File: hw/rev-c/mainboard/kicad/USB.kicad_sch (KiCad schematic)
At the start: 6 parts, among them J24 USB1.1_HOST_TYPE_C

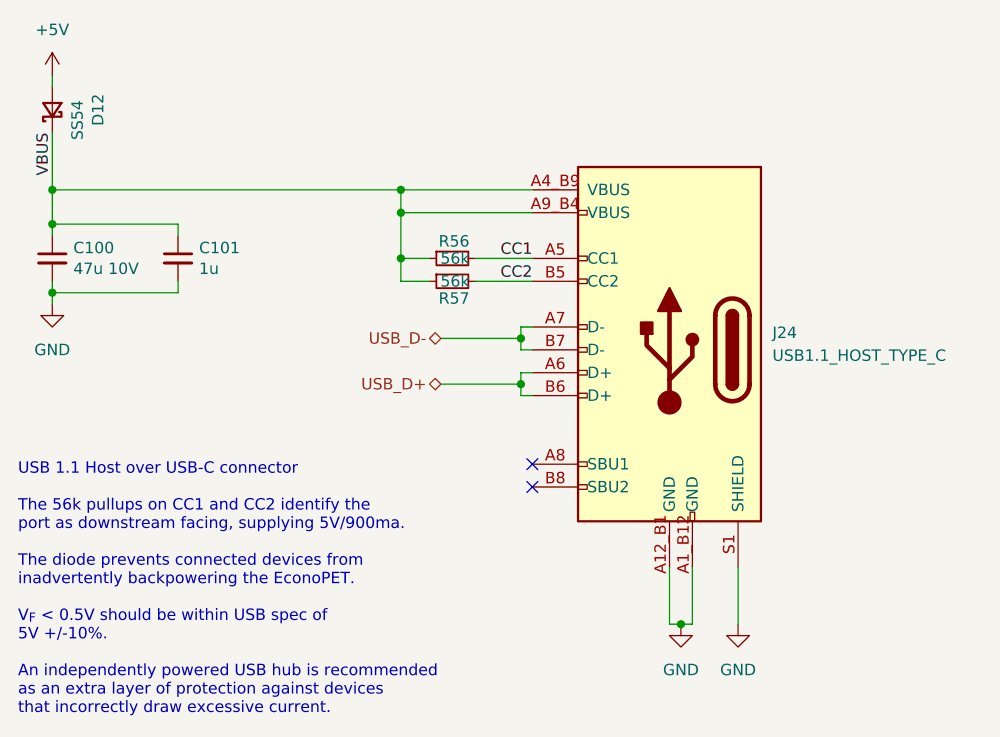
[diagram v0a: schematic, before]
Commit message: hw: fix wire/grid violations in schematic
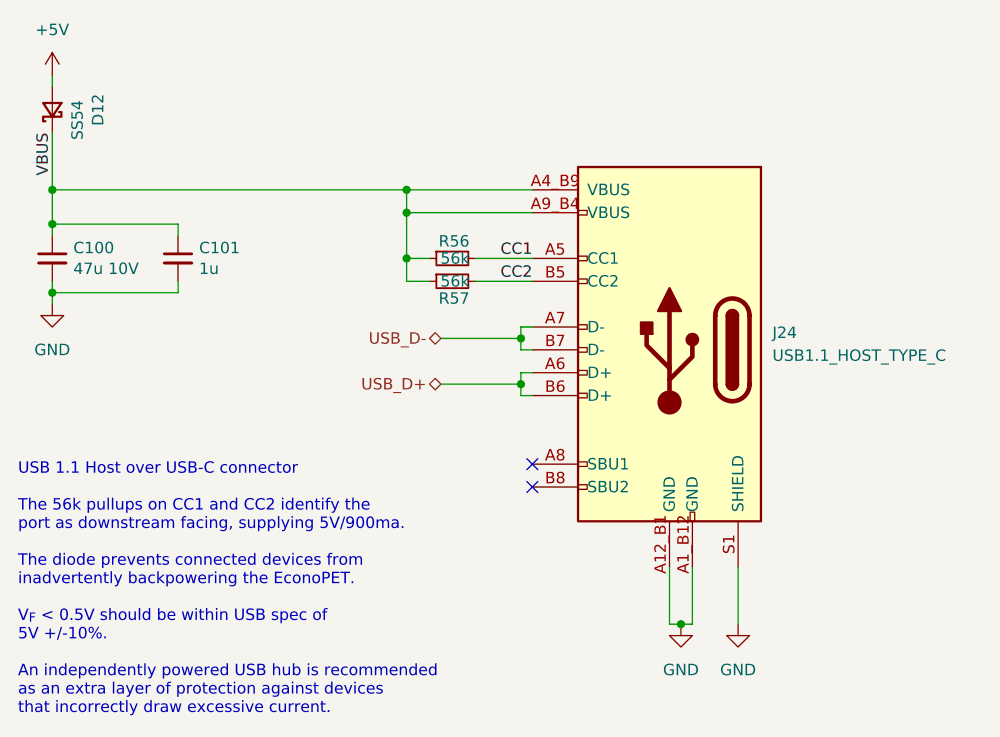
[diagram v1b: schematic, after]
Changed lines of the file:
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@@
+	)
+	(junction
+		(at 123.19 82.55)
+		(diameter 0)
+		(color 0 0 0 0)
 	)
 	(junction
@@
 	)
 	(junction
-		(at 122.555 77.47)
+		(at 123.19 77.47)
 		(diameter 0)
 		(color 0 0 0 0)
@@
 	)
 	(junction
-		(at 122.555 82.55)
-		(diameter 0)
-		(color 0 0 0 0)
-	)
-	(junction
-		(at 122.555 74.93)
+		(at 123.19 74.93)
 		(diameter 0)
 		(color 0 0 0 0)
@@
 	(wire
 		(pts
+			(xy 123.19 74.93) (xy 137.16 74.93)
+		)
+		(stroke
+			(width 0)
+			(type default)
+		)
+	)
+	(wire
+		(pts
 			(xy 137.16 95.25) (xy 135.89 95.25)
 		)
@@
 	(wire
 		(pts
-			(xy 122.555 77.47) (xy 137.16 77.47)
+			(xy 123.19 82.55) (xy 125.73 82.55)
 		)
 		(stroke
@@
 	(wire
 		(pts
-			(xy 122.555 82.55) (xy 122.555 77.47)
+			(xy 123.19 82.55) (xy 123.19 77.47)
 		)
 		(stroke
@@
 	(wire
 		(pts
-			(xy 83.82 74.93) (xy 122.555 74.93)
+			(xy 83.82 74.93) (xy 123.19 74.93)
 		)
 		(stroke
@@
 	(wire
 		(pts
-			(xy 122.555 85.09) (xy 122.555 82.55)
-		)
-		(stroke
-			(width 0)
-			(type default)
-		)
-	)
-	(wire
-		(pts
-			(xy 122.555 82.55) (xy 125.73 82.55)
+			(xy 123.19 85.09) (xy 123.19 82.55)
+		)
+		(stroke
+			(width 0)
+			(type default)
+		)
+	)
+	(wire
+		(pts
+			(xy 123.19 77.47) (xy 137.16 77.47)
 		)
 		(stroke
@@
 	(wire
 		(pts
-			(xy 122.555 77.47) (xy 122.555 74.93)
+			(xy 123.19 77.47) (xy 123.19 74.93)
 		)
 		(stroke
@@
 	(wire
 		(pts
-			(xy 122.555 74.93) (xy 137.16 74.93)
-		)
-		(stroke
-			(width 0)
-			(type default)
-		)
-	)
-	(wire
-		(pts
 			(xy 153.67 123.19) (xy 154.94 123.19)
 		)
@@
 	(wire
 		(pts
-			(xy 125.73 85.09) (xy 122.555 85.09)
-		)
-		(stroke
+			(xy 125.73 85.09) (xy 123.19 85.09)
+		)
+		(stroke

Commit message: hw: update usb-c receptical symbol
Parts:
- J24: symbol JLCPCB:USB_C_Receptacle_USB2.0 -> EconoPET:USB_C_Receptacle_USB2.0
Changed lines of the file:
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@@
 	)
 	(symbol
-		(lib_id "JLCPCB:USB_C_Receptacle_USB2.0")
+		(lib_id "EconoPET:USB_C_Receptacle_USB2.0")
 		(at 152.4 92.71 0)
 		(mirror y)

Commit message: hw: renumber reference designators
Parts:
- renumbered C100 to C101, C101 to C102, J24 to J25, R56 to R61, R57 to R62
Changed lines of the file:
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@@
 		(on_board yes)
 		(dnp no)
-		(property "Reference" "C101"
+		(property "Reference" "C102"
 			(at 100.1268 81.3816 0)
 			(effects
@@
 			(project ""
 				(path "/2eea20e6-112c-411a-b615-885ae773135a/00000000-0000-0000-0000-0000617d6918/b70241ab-8a5c-42d5-a1ab-8f4bc50a1197/6521fafb-cb3f-4004-93ad-439f568f7908"
-					(reference "C101")
+					(reference "C102")
 					(unit 1)
 				)
@@
 		(dnp no)
 		(fields_autoplaced yes)
-		(property "Reference" "#PWR0171"
+		(property "Reference" "#PWR0172"
 			(at 83.82 93.98 0)
 			(effects
@@
 			(project ""
 				(path "/2eea20e6-112c-411a-b615-885ae773135a/00000000-0000-0000-0000-0000617d6918/b70241ab-8a5c-42d5-a1ab-8f4bc50a1197/6521fafb-cb3f-4004-93ad-439f568f7908"
-					(reference "#PWR0171")
+					(reference "#PWR0172")
 					(unit 1)
 				)
@@
 		(dnp no)
 		(fields_autoplaced yes)
-		(property "Reference" "J24"
+		(property "Reference" "J25"
 			(at 163.83 90.8049 0)
 			(effects
@@
 			(project ""
 				(path "/2eea20e6-112c-411a-b615-885ae773135a/00000000-0000-0000-0000-0000617d6918/b70241ab-8a5c-42d5-a1ab-8f4bc50a1197/6521fafb-cb3f-4004-93ad-439f568f7908"
-					(reference "J24")
+					(reference "J25")
 					(unit 1)
 				)
@@
 		(on_board yes)
 		(dnp no)
-		(property "Reference" "R57"
+		(property "Reference" "R62"
 			(at 130.175 86.995 90)
 			(effects
@@
 			(project ""
 				(path "/2eea20e6-112c-411a-b615-885ae773135a/00000000-0000-0000-0000-0000617d6918/b70241ab-8a5c-42d5-a1ab-8f4bc50a1197/6521fafb-cb3f-4004-93ad-439f568f7908"
-					(reference "R57")
+					(reference "R62")
 					(unit 1)
 				)
@@
 		(on_board yes)
 		(dnp no)
-		(property "Reference" "C100"
+		(property "Reference" "C101"
 			(at 86.1568 81.3816 0)
 			(effects
@@
 			(project ""
 				(path "/2eea20e6-112c-411a-b615-885ae773135a/00000000-0000-0000-0000-0000617d6918/b70241ab-8a5c-42d5-a1ab-8f4bc50a1197/6521fafb-cb3f-4004-93ad-439f568f7908"
-					(reference "C100")
+					(reference "C101")
 					(unit 1)
 				)
@@
 		(dnp no)
 		(fields_autoplaced yes)
-		(property "Reference" "#PWR0170"
+		(property "Reference" "#PWR0171"
 			(at 83.82 66.04 0)
 			(effects
@@
 			(project ""
 				(path "/2eea20e6-112c-411a-b615-885ae773135a/00000000-0000-0000-0000-0000617d6918/b70241ab-8a5c-42d5-a1ab-8f4bc50a1197/6521fafb-cb3f-4004-93ad-439f568f7908"
-					(reference "#PWR0170")
+					(reference "#PWR0171")
 					(unit 1)
 				)
@@
 		(on_board yes)
 		(dnp no)
-		(property "Reference" "R56"
+		(property "Reference" "R61"
 			(at 130.175 80.645 90)
 			(effects
@@
 			(project ""
 				(path "/2eea20e6-112c-411a-b615-885ae773135a/00000000-0000-0000-0000-0000617d6918/b70241ab-8a5c-42d5-a1ab-8f4bc50a1197/6521fafb-cb3f-4004-93ad-439f568f7908"
-					(reference "R56")
+					(reference "R61")
 					(unit 1)
 				)
@@
 		(dnp no)
 		(fields_autoplaced yes)
-		(property "Reference" "#PWR0172"
+		(property "Reference" "#PWR0173"
 			(at 153.67 129.54 0)
 			(effects
@@
 			(project ""
 				(path "/2eea20e6-112c-411a-b615-885ae773135a/00000000-0000-0000-0000-0000617d6918/b70241ab-8a5c-42d5-a1ab-8f4bc50a1197/6521fafb-cb3f-4004-93ad-439f568f7908"
-					(reference "#PWR0172")
+					(reference "#PWR0173")
 					(unit 1)
 				)
@@
 		(dnp no)
 		(fields_autoplaced yes)
-		(property "Reference" "#PWR0173"
+		(property "Reference" "#PWR0174"
 			(at 160.02 129.54 0)
 			(effects
@@
 			(project ""
 				(path "/2eea20e6-112c-411a-b615-885ae773135a/00000000-0000-0000-0000-0000617d6918/b70241ab-8a5c-42d5-a1ab-8f4bc50a1197/6521fafb-cb3f-4004-93ad-439f568f7908"
-					(reference "#PWR0173")
-					(unit 1)
-				)
+					(reference "#PWR0174")
+					(unit 1)
+				)

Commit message: hw: match original PET designators for connectors
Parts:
- renumbered C101 to C102, C102 to C103, J25 to J26, R61 to R63, R62 to R64
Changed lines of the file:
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@@
 		(on_board yes)
 		(dnp no)
-		(property "Reference" "C102"
+		(property "Reference" "C103"
 			(at 100.1268 81.3816 0)
 			(effects
@@
 			(project ""
 				(path "/2eea20e6-112c-411a-b615-885ae773135a/00000000-0000-0000-0000-0000617d6918/b70241ab-8a5c-42d5-a1ab-8f4bc50a1197/6521fafb-cb3f-4004-93ad-439f568f7908"
-					(reference "C102")
+					(reference "C103")
 					(unit 1)
 				)
@@
 		(dnp no)
 		(fields_autoplaced yes)
-		(property "Reference" "J25"
+		(property "Reference" "J26"
 			(at 163.83 90.8049 0)
 			(effects
@@
 			(project ""
 				(path "/2eea20e6-112c-411a-b615-885ae773135a/00000000-0000-0000-0000-0000617d6918/b70241ab-8a5c-42d5-a1ab-8f4bc50a1197/6521fafb-cb3f-4004-93ad-439f568f7908"
-					(reference "J25")
+					(reference "J26")
 					(unit 1)
 				)
@@
 		(on_board yes)
 		(dnp no)
-		(property "Reference" "R62"
+		(property "Reference" "R64"
 			(at 130.175 86.995 90)
 			(effects
@@
 			(project ""
 				(path "/2eea20e6-112c-411a-b615-885ae773135a/00000000-0000-0000-0000-0000617d6918/b70241ab-8a5c-42d5-a1ab-8f4bc50a1197/6521fafb-cb3f-4004-93ad-439f568f7908"
-					(reference "R62")
+					(reference "R64")
 					(unit 1)
 				)
@@
 		(on_board yes)
 		(dnp no)
-		(property "Reference" "C101"
+		(property "Reference" "C102"
 			(at 86.1568 81.3816 0)
 			(effects
@@
 			(project ""
 				(path "/2eea20e6-112c-411a-b615-885ae773135a/00000000-0000-0000-0000-0000617d6918/b70241ab-8a5c-42d5-a1ab-8f4bc50a1197/6521fafb-cb3f-4004-93ad-439f568f7908"
-					(reference "C101")
+					(reference "C102")
 					(unit 1)
 				)
@@
 		(on_board yes)
 		(dnp no)
-		(property "Reference" "R61"
+		(property "Reference" "R63"
 			(at 130.175 80.645 90)
 			(effects
@@
 			(project ""
 				(path "/2eea20e6-112c-411a-b615-885ae773135a/00000000-0000-0000-0000-0000617d6918/b70241ab-8a5c-42d5-a1ab-8f4bc50a1197/6521fafb-cb3f-4004-93ad-439f568f7908"
-					(reference "R61")
-					(unit 1)
-				)
+					(reference "R63")
+					(unit 1)
+				)
